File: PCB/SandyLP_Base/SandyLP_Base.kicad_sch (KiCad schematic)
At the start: 173 parts, among them J1 Conn_02x02_Top_Bottom, J11 Conn_02x02_Odd_Even, J2 Conn_02x02_Top_Bottom, J3 Conn_02x02_Top_Bottom, J4 Conn_02x02_Top_Bottom, J5 Conn_02x02_Top_Bottom, J6 Conn_02x02_Top_Bottom, J7 USB_C_Receptacle_USB2.0, J8 Conn_01x03, J9 Conn_01x08_Pin, Q1 BSS138, SW1 BOOT, SW2 RESET, U1 NCP1117-3.3_SOT223, U2 RP2040, U3 W25Q128JVPIQ, Y1 12MHz

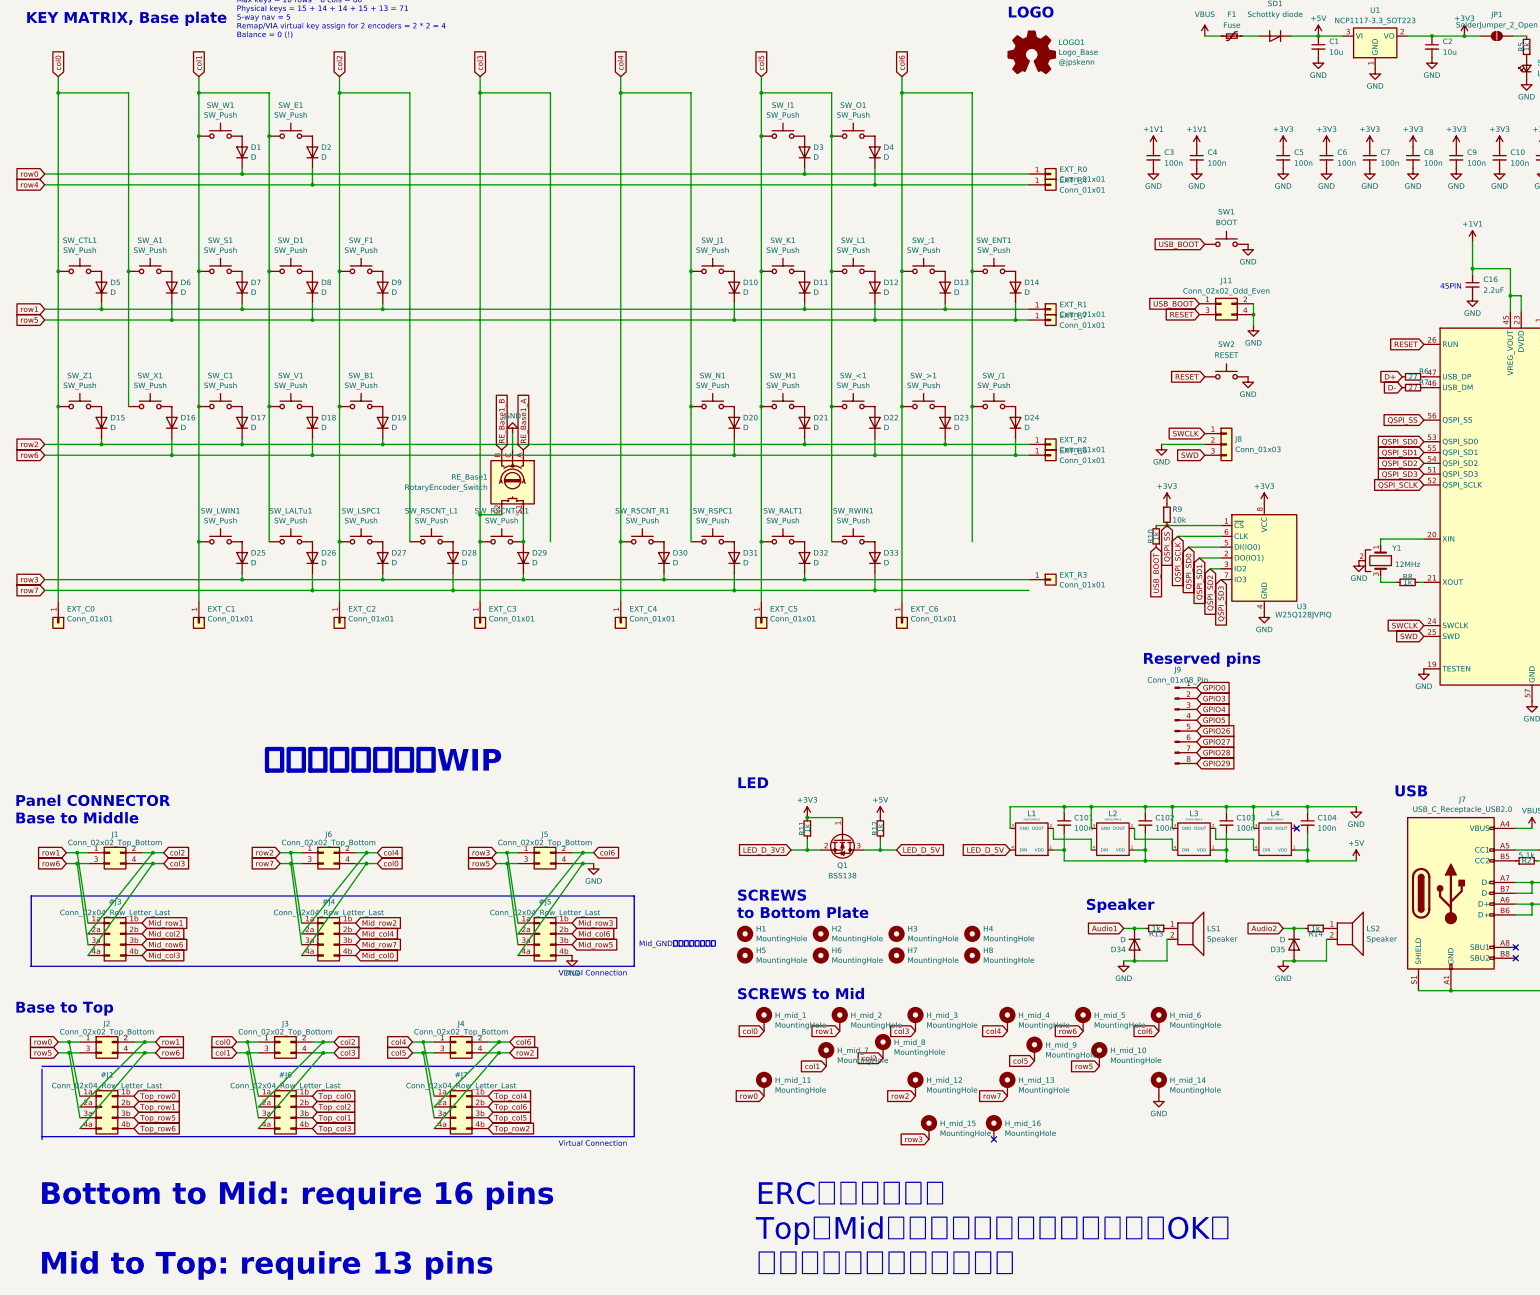
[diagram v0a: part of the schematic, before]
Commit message: 回路図編集：基板間接続、ネジ、フットプリント指定
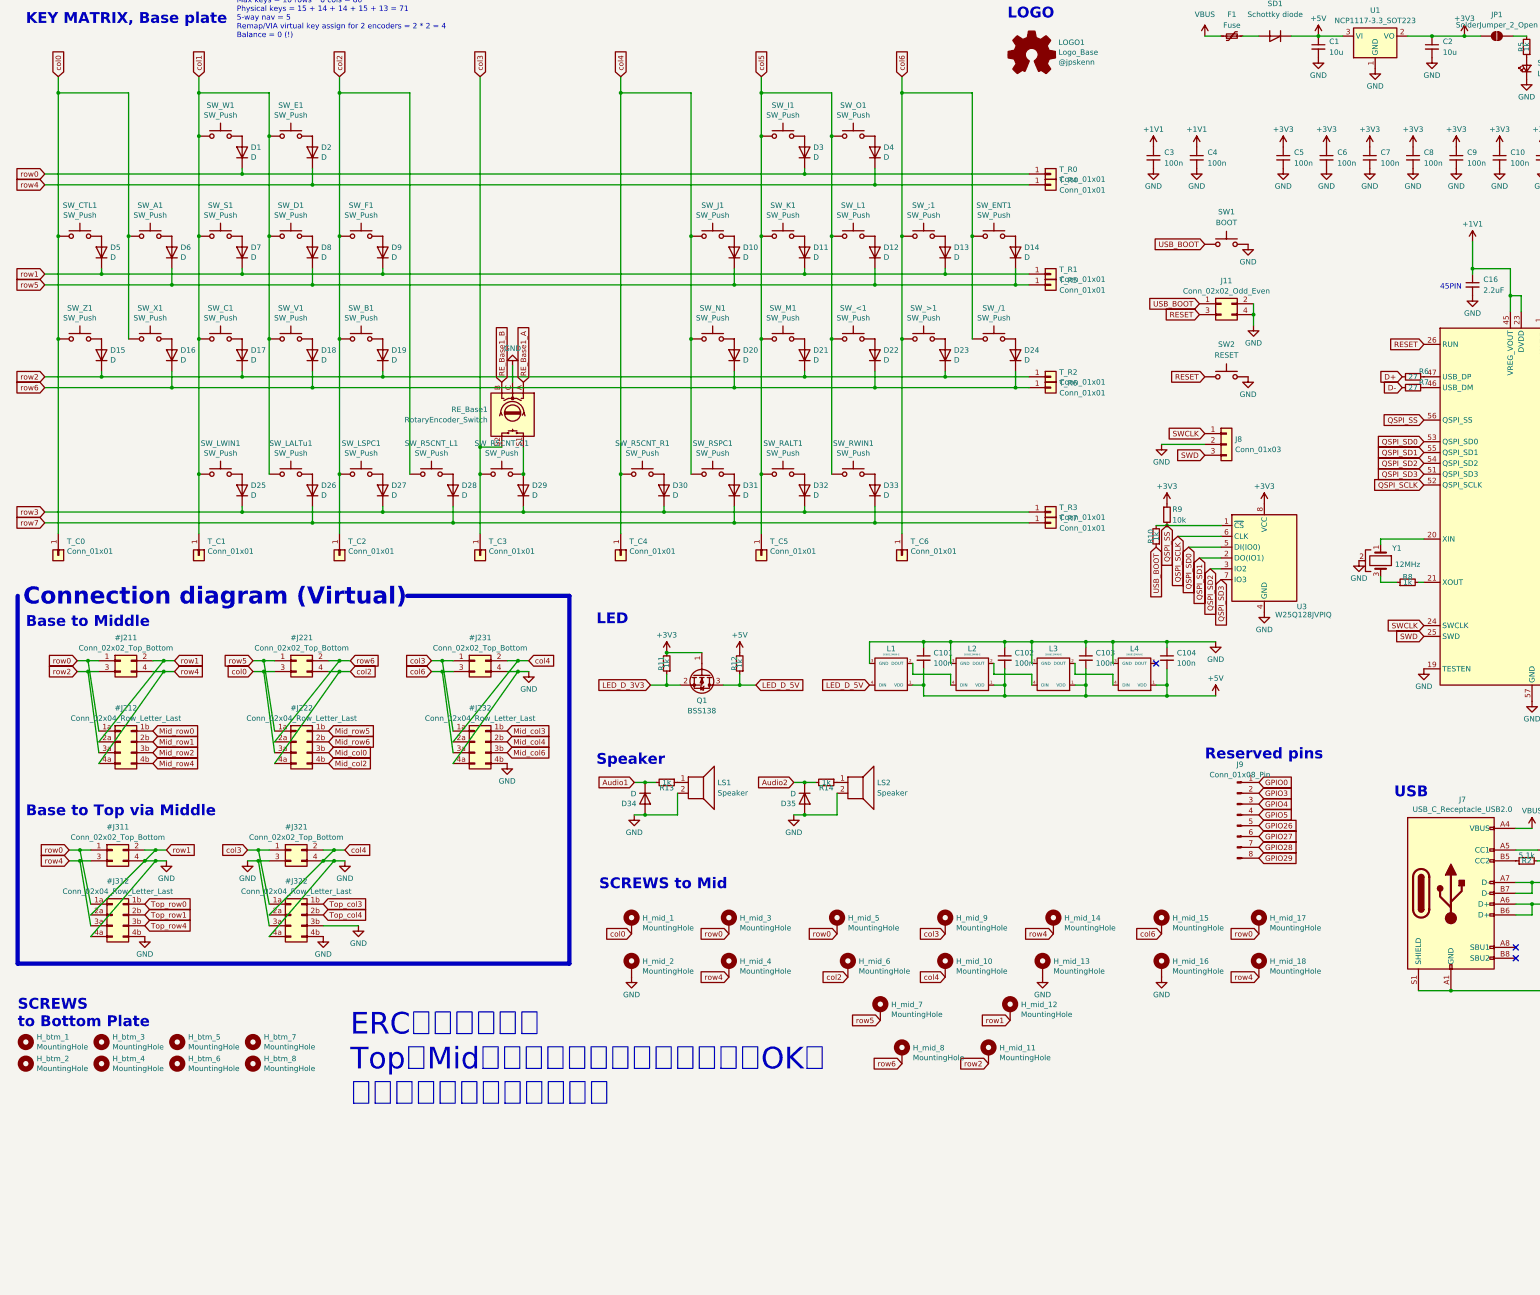
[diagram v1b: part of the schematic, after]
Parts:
- removed #J7: Conn_02x04_Row_Letter_Last, symbol Connector_Generic:Conn_02x04_Row_Letter_Last
- removed H_mid_13, H_mid_15, H_mid_7, H_mid_9: MountingHole, locallib:MountingHole_2.2mm_M2_Pad_minimal, symbol Mechanical:MountingHole_Pad
- removed J4: Conn_02x02_Top_Bottom, locallib:JST_SH_SM04B-SRSS-TB_1x04-1MP_P1.00mm_Horizontal_wCable_housing_spare_pin_courtyard, symbol Connector_Generic:Conn_02x02_Odd_Even
- added H_mid_14, H_mid_17, H_mid_18, H_mid_2, H_mid_3, H_mid_4: MountingHole, locallib:MountingHole_1.8-2.2mm_M2_Pad_minimal, symbol Mechanical:MountingHole_Pad
- added T_R7: Conn_01x01, locallib:TestPoint_THTPad_D2.0mm_Drill1.0mm, symbol Connector_Generic:Conn_01x01
- H_mid_1, H_mid_16: footprint locallib:MountingHole_2.2mm_M2_Pad_minimal -> locallib:MountingHole_1.8-2.2mm_M2_Pad_minimal
- H_mid_10: renamed from H_mid_4; footprint locallib:MountingHole_2.2mm_M2_Pad_minimal -> locallib:MountingHole_1.8-2.2mm_M2_Pad_minimal
- H_mid_11: renamed from H_mid_12; footprint locallib:MountingHole_2.2mm_M2_Pad_minimal -> locallib:MountingHole_1.8-2.2mm_M2_Pad_minimal
- H_mid_12: renamed from H_mid_2; footprint locallib:MountingHole_2.2mm_M2_Pad_minimal -> locallib:MountingHole_1.8-2.2mm_M2_Pad_minimal
- H_mid_13: renamed from H_mid_14; footprint locallib:MountingHole_2.2mm_M2_Pad_minimal -> locallib:MountingHole_1.8-2.2mm_M2_Pad_minimal
- H_mid_15: renamed from H_mid_6; footprint locallib:MountingHole_2.2mm_M2_Pad_minimal -> locallib:MountingHole_1.8-2.2mm_M2_Pad_minimal
- H_mid_5: renamed from H_mid_11; footprint locallib:MountingHole_2.2mm_M2_Pad_minimal -> locallib:MountingHole_1.8-2.2mm_M2_Pad_minimal
- H_mid_6: renamed from H_mid_8; footprint locallib:MountingHole_2.2mm_M2_Pad_minimal -> locallib:MountingHole_1.8-2.2mm_M2_Pad_minimal
- H_mid_7: renamed from H_mid_10; footprint locallib:MountingHole_2.2mm_M2_Pad_minimal -> locallib:MountingHole_1.8-2.2mm_M2_Pad_minimal
- H_mid_8: renamed from H_mid_5; footprint locallib:MountingHole_2.2mm_M2_Pad_minimal -> locallib:MountingHole_1.8-2.2mm_M2_Pad_minimal
- H_mid_9: renamed from H_mid_3; footprint locallib:MountingHole_2.2mm_M2_Pad_minimal -> locallib:MountingHole_1.8-2.2mm_M2_Pad_minimal
- renumbered J1 to #J211, #J3 to #J212, J6 to #J221, #J4 to #J222, J5 to #J231, #J5 to #J232, J2 to #J311, #J1 to #J312, J3 to #J321, #J6 to #J322, H1 to H_btm_1, H5 to H_btm_2, H2 to H_btm_3, H6 to H_btm_4, H3 to H_btm_5, H7 to H_btm_6, H4 to H_btm_7, H8 to H_btm_8, EXT_C0 to T_C0, EXT_C1 to T_C1, EXT_C2 to T_C2, EXT_C3 to T_C3, EXT_C4 to T_C4, EXT_C5 to T_C5, EXT_C6 to T_C6, EXT_R0 to T_R0, EXT_R1 to T_R1, EXT_R2 to T_R2, EXT_R3 to T_R3, EXT_R4 to T_R4, EXT_R7 to T_R5, EXT_R6 to T_R6
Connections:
- net Mid_row3 is gone; now on net Mid_col3: #J232.1b (Pin_1b)
- net Mid_row7 is gone; now on net Mid_col0: #J222.3b (Pin_3b)
- net Top_col0 is gone; now on net Top_col3: #J322.1b (Pin_1b)
- net Top_col1 is gone; now on net GND: #J322.3b (Pin_3b)
- net Top_col2 is gone; now on net Top_col4: #J322.2b (Pin_2b)
- net Top_row6 is gone; now on net GND: #J312.4b (Pin_4b)
- net GND: now also #J211.2 (Pin_2), #J212.2a (Pin_2a), #J231.2 (Pin_2), #J232.2a (Pin_2a), #J311.2 (Pin_2), #J311.4 (Pin_4), #J312.2a (Pin_2a), #J312.4a (Pin_4a), #J321.2 (Pin_2), #J321.3 (Pin_3), #J321.4 (Pin_4), #J322.2a (Pin_2a), #J322.3a (Pin_3a), #J322.4a (Pin_4a), #J322.4b (Pin_4b), D11.1 (K), D13.1 (K), D5.1 (K), D7.1 (K), D9.1 (K), H_mid_10.1, H_mid_12.1, H_mid_16.1, SW_J1.1, SW_N1.1, SW_R5CNT_R1.1, SW_RSPC1.1, T_C4.1 (Pin_1), T_R1.1 (Pin_1), U2.11 (GPIO8), U2.3 (GPIO1), H_mid_2.1
- net Mid_col0: no longer #J222.4b (Pin_4b)
- net Mid_col2: now also #J222.4b (Pin_4b); no longer #J212.2b (Pin_2b)
- net Mid_col3: no longer #J212.4b (Pin_4b)
- net Mid_col4: now also #J232.2b (Pin_2b); no longer #J222.2b (Pin_2b)
- net Mid_col6: now also #J232.3b (Pin_3b); no longer #J232.2b (Pin_2b)
- net Mid_row1: now also #J212.2b (Pin_2b); no longer #J212.1b (Pin_1b)
- net Mid_row2: now also #J212.3b (Pin_3b); no longer #J222.1b (Pin_1b)
- net Mid_row5: now also #J222.1b (Pin_1b); no longer #J232.3b (Pin_3b)
- net Mid_row6: now also #J222.2b (Pin_2b); no longer #J212.3b (Pin_3b)
- net Top_col3: no longer #J322.4b (Pin_4b)
- net col0: now also #J221.3 (Pin_3), #J222.3a (Pin_3a); no longer #J221.4 (Pin_4), #J222.4a (Pin_4a), #J321.1 (Pin_1), #J322.1a (Pin_1a)
- net col1: no longer #J321.3 (Pin_3), #J322.3a (Pin_3a)
- net col2: now also #J221.4 (Pin_4), #J222.4a (Pin_4a); no longer #J211.2 (Pin_2), #J212.2a (Pin_2a), #J321.2 (Pin_2), #J322.2a (Pin_2a)
- net col3: now also #J231.1 (Pin_1), #J232.1a (Pin_1a), #J321.1 (Pin_1), #J322.1a (Pin_1a); no longer #J211.4 (Pin_4), #J212.4a (Pin_4a), #J321.4 (Pin_4), #J322.4a (Pin_4a)
- net col6: now also #J231.3 (Pin_3), #J232.3a (Pin_3a); no longer #J231.2 (Pin_2), #J232.2a (Pin_2a)
- net row0: now also #J211.1 (Pin_1), #J212.1a (Pin_1a), H_mid_17.1, H_mid_3.1
- net row2: now also #J211.3 (Pin_3), #J212.3a (Pin_3a); no longer #J221.1 (Pin_1), #J222.1a (Pin_1a)
- net row3: no longer #J231.1 (Pin_1), #J232.1a (Pin_1a)
- net row4: now also #J211.4 (Pin_4), #J212.4a (Pin_4a), #J311.3 (Pin_3), #J312.3a (Pin_3a), H_mid_14.1, H_mid_18.1, H_mid_4.1
- net row5: now also #J221.1 (Pin_1), #J222.1a (Pin_1a); no longer #J231.3 (Pin_3), #J232.3a (Pin_3a), #J311.3 (Pin_3), #J312.3a (Pin_3a)
- net row6: now also #J221.2 (Pin_2), #J222.2a (Pin_2a); no longer #J211.3 (Pin_3), #J212.3a (Pin_3a), #J311.4 (Pin_4), #J312.4a (Pin_4a)
- net row7: now also T_R7.1 (Pin_1); no longer #J221.3 (Pin_3), #J222.3a (Pin_3a)
- net Top_row5 renamed Top_row4
- removed net col4: #J221.2 (Pin_2), #J222.2a (Pin_2a), H_mid_10.1, SW_J1.1, SW_N1.1, SW_R5CNT_R1.1, SW_RSPC1.1, T_C4.1 (Pin_1), U2.3 (GPIO1)
- removed net row1: #J211.1 (Pin_1), #J212.1a (Pin_1a), #J311.2 (Pin_2), #J312.2a (Pin_2a), D11.1 (K), D13.1 (K), D5.1 (K), D7.1 (K), D9.1 (K), H_mid_12.1, T_R1.1 (Pin_1), U2.11 (GPIO8)
- new net Mid_row0: #J212.1b (Pin_1b)
- new net Mid_row4: #J212.4b (Pin_4b)
- no-connect marks 4 -> 3
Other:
- note added: "Base to Middle"
- note added: "Base to Top via Middle"
- note added: "Connection diagram (Virtual)"
- note removed: "Base to Top"
- note removed: "Bottom to Mid: require 16 pins Mid to Top: require 13 pins"
- note removed: "Mid_GNDを仮につけている"
- note removed: "Panel CONNECTOR Base to Middle"
- note removed: "Virtual Connection"
- note removed: "コネクタとネジはWIP"
- moved on the sheet: C101, C102, C103, C104, D10, D11, D12, D13, D14, D15, D16, D17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

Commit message: Base外形作成。ネジ配置。
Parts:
- removed J9: Conn_01x08_Pin, locallib:PinHeader_1x08_P1.00mm_Vertical_All_circle, symbol Connector:Conn_01x08_Pin
- added J1: Conn_01x09_Pin, symbol Connector:Conn_01x09_Pin
- renumbered H_mid_6 to H_mid_10, H_mid_10 to H_mid_11, H_mid_13 to H_mid_12, H_mid_16 to H_mid_13, H_mid_18 to H_mid_14, H_mid_7 to H_mid_15, H_mid_12 to H_mid_16, H_mid_8 to H_mid_17, H_mid_11 to H_mid_18, H_mid_3 to H_mid_2, H_mid_5 to H_mid_3, H_mid_9 to H_mid_4, H_mid_14 to H_mid_5, H_mid_15 to H_mid_6, H_mid_17 to H_mid_7, H_mid_2 to H_mid_8, H_mid_4 to H_mid_9
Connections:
- net GND: now also H_mid_14.1; no longer #J211.2 (Pin_2), #J212.2a (Pin_2a), #J231.2 (Pin_2), #J232.2a (Pin_2a), #J311.2 (Pin_2), #J312.2a (Pin_2a), #J321.2 (Pin_2), #J322.2a (Pin_2a), D11.1 (K), D13.1 (K), D5.1 (K), D7.1 (K), D9.1 (K), H_mid_11.1, H_mid_13.1, H_mid_16.1, SW_J1.1, SW_N1.1, SW_R5CNT_R1.1, SW_RSPC1.1, T_C4.1 (Pin_1), T_R1.1 (Pin_1), U2.11 (GPIO8), U2.3 (GPIO1)
- net GPIO0: now also J1.1 (Pin_1)
- net GPIO14: now also J1.5 (Pin_5)
- net GPIO26: now also J1.6 (Pin_6)
- net GPIO27: now also J1.7 (Pin_7)
- net GPIO28: now also J1.8 (Pin_8)
- net GPIO29: now also J1.9 (Pin_9)
- net GPIO3: now also J1.2 (Pin_2)
- net GPIO4: now also J1.3 (Pin_3)
- net GPIO5: now also J1.4 (Pin_4)
- net col6: now also H_mid_7.1; no longer H_mid_6.1
- net row0: now also H_mid_6.1; no longer H_mid_7.1
- net row4: now also H_mid_13.1; no longer H_mid_14.1
- new net col4: #J231.2 (Pin_2), #J232.2a (Pin_2a), #J321.2 (Pin_2), #J322.2a (Pin_2a), H_mid_11.1, SW_J1.1, SW_N1.1, SW_R5CNT_R1.1, SW_RSPC1.1, T_C4.1 (Pin_1), U2.3 (GPIO1)
- new net row1: #J211.2 (Pin_2), #J212.2a (Pin_2a), #J311.2 (Pin_2), #J312.2a (Pin_2a), D11.1 (K), D13.1 (K), D5.1 (K), D7.1 (K), D9.1 (K), H_mid_16.1, T_R1.1 (Pin_1), U2.11 (GPIO8)

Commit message: WIP パーツ配置
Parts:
- removed C101, C102, C103, C104: 100n, Capacitor_SMD:C_0402_1005Metric, symbol Device:C_Small
- added C14, C15, C18, C19, C20, C21: 100n, Capacitor_SMD:C_0402_1005Metric, symbol Device:C_Small
- added L5, L6: SK6812MINI-E, locallib:YS-SK6812MINI-E_middle_hole_with_small_pad, symbol kbd:SK6812MINI-E
- J1: footprint (none) -> Connector_PinHeader_1.00mm:PinHeader_1x09_P1.00mm_Vertical
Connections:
- net +5V: now also C14.2, C15.2, C18.2, C19.2, C20.2, C21.2, L5.1 (VDD), L6.1 (VDD)
- net GND: now also C14.1, C15.1, C18.1, C19.1, C20.1, C21.1, L5.3 (GND), L6.3 (GND)
- net LED_D_5V_CONNECTION: now reaches L3.2 (DOUT), L4.4 (DIN)
- net at L4.2 (DOUT): now also L5.4 (DIN)
- new net: L5.2 (DOUT), L6.4 (DIN)

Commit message: USBコネクタ周りの配線に合わせて、Mid孤立部分のネジへのピン割り当てを変更。
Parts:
- LOGO1: footprint Jones.local:Sandy_logo_w60_new -> locallib:SandyLP_logo_w60
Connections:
- net GND: now also H_mid_13.1, H_mid_9.1; no longer H_mid_14.1, H_mid_8.1
- net row4: now also H_mid_14.1, H_mid_8.1; no longer H_mid_13.1, H_mid_9.1
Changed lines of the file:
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@@
 	(global_label "row4"
 		(shape input)
-		(at 180.34 243.84 180)
+		(at 157.48 243.84 180)
 		(fields_autoplaced yes)
 		(effects
@@
 		)
 		(property "Intersheetrefs" "${INTERSHEET_REFS}"
-			(at 173.5338 243.84 0)
+			(at 150.6738 243.84 0)
 			(effects
 				(font
@@
 		)
 		(property "シート間のリファレンス" "${INTERSHEET_REFS}"
-			(at 180.34 245.6752 0)
+			(at 157.48 245.6752 0)
 			(effects
 				(font
@@
 	(global_label "row4"
 		(shape input)
-		(at 281.94 243.84 180)
+		(at 304.8 243.84 180)
 		(fields_autoplaced yes)
 		(effects
@@
 		)
 		(property "Intersheetrefs" "${INTERSHEET_REFS}"
-			(at 275.1338 243.84 0)
+			(at 297.9938 243.84 0)
 			(effects
 				(font
@@
 		)
 		(property "シート間のリファレンス" "${INTERSHEET_REFS}"
-			(at 281.94 245.6752 0)
+			(at 304.8 245.6752 0)
 			(effects
 				(font
@@
 			)
 		)
-		(property "Footprint" "Jones.local:Sandy_logo_w60_new"
+		(property "Footprint" "locallib:SandyLP_logo_w60"
 			(at 251.46 27.305 0)
 			(effects
@@
 	(symbol
 		(lib_id "power:GND")
-		(at 304.8 243.84 0)
+		(at 281.94 243.84 0)
 		(unit 1)
 		(exclude_from_sim no)
@@
 		(fields_autoplaced yes)
 		(property "Reference" "#PWR067"
-			(at 304.8 250.19 0)
+			(at 281.94 250.19 0)
 			(effects
 				(font
@@
 		)
 		(property "Value" "GND"
-			(at 304.8 247.9731 0)
+			(at 281.94 247.9731 0)
 			(effects
 				(font
@@
 		)
 		(property "Footprint" ""
-			(at 304.8 243.84 0)
+			(at 281.94 243.84 0)
 			(effects
 				(font
@@
 		)
 		(property "Datasheet" ""
-			(at 304.8 243.84 0)
+			(at 281.94 243.84 0)
 			(effects
 				(font
@@
 		)
 		(property "Description" "Power symbol creates a global label with name \"GND\" , ground"
-			(at 304.8 243.84 0)
+			(at 281.94 243.84 0)
 			(effects
 				(font
@@
 	(symbol
 		(lib_id "power:GND")
-		(at 157.48 243.84 0)
+		(at 180.34 243.84 0)
 		(unit 1)
 		(exclude_from_sim no)
@@
 		(fields_autoplaced yes)
 		(property "Reference" "#PWR066"
-			(at 157.48 250.19 0)
+			(at 180.34 250.19 0)
 			(effects
 				(font
@@
 		)
 		(property "Value" "GND"
-			(at 157.48 247.9731 0)
+			(at 180.34 247.9731 0)
 			(effects
 				(font
@@
 		)
 		(property "Footprint" ""
-			(at 157.48 243.84 0)
+			(at 180.34 243.84 0)
 			(effects
 				(font
@@
 		)
 		(property "Datasheet" ""
-			(at 157.48 243.84 0)
+			(at 180.34 243.84 0)
 			(effects
 				(font
@@
 		)
 		(property "Description" "Power symbol creates a global label with name \"GND\" , ground"
-			(at 157.48 243.84 0)
+			(at 180.34 243.84 0)
 			(effects
 				(font

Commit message: 配線完了。ビア打ちまだ。
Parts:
- removed J1: Conn_01x09_Pin, Connector_PinHeader_1.00mm:PinHeader_1x09_P1.00mm_Vertical, symbol Connector:Conn_01x09_Pin
- removed SW_R5CNT_C1: SW_Push, locallib:Kailh_socket_ChocV2, symbol Switch:SW_Push
- added H_btm_5, H_btm_6, H_btm_7: MountingHole, locallib:MountingHole_2.2mm_M2_No_Cu, symbol Mechanical:MountingHole
- added J1: Conn_01x10_Pin, Connector_PinHeader_1.00mm:PinHeader_1x10_P1.00mm_Vertical, symbol Connector:Conn_01x10_Pin
- SW1, SW2: footprint Button_Switch_SMD:SW_SPST_PTS810 -> Button_Switch_SMD:SW_SPST_TL3342
- SW_R5CNT_C1: renamed from RE_Base1; footprint locallib:RotaryEncoder_Alps_EC11K-Switch_Vertical_H20mm_NPTH_MP_minimal -> locallib:ChocV2_AND_RotaryEncoder_Alps_EC11K-Switch_Vertical_H20mm_NPTH_MP_minimal
- renumbered J11 to #J11, H_btm_6 to H_btm_10, H_btm_8 to H_btm_11, H_btm_3 to H_btm_2, H_btm_5 to H_btm_3, H_btm_7 to H_btm_4, H_btm_2 to H_btm_8, H_btm_4 to H_btm_9
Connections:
- net GPIO0 is gone; now on net GPIO29: U2.41 (GPIO29_ADC3)
- net GPIO14 is gone; now on net LED_D_3V3: U2.30 (GPIO19)
- net GPIO3 is gone; now on net GPIO28: U2.40 (GPIO28_ADC2)
- net GPIO4 is gone; now on net GPIO27: U2.39 (GPIO27_ADC1)
- net Audio1: now also U2.29 (GPIO18); no longer U2.31 (GPIO20)
- net Audio2: now also U2.15 (GPIO12); no longer U2.13 (GPIO10)
- net GPIO26: now also U2.38 (GPIO26_ADC0), J1.7 (Pin_7); no longer U2.37 (GPIO25)
- net GPIO27: now also J1.8 (Pin_8); no longer U2.36 (GPIO24)
- net GPIO28: now also J1.9 (Pin_9); no longer U2.35 (GPIO23)
- net GPIO29: now also J1.10 (Pin_10); no longer U2.34 (GPIO22)
- net LED_D_3V3: no longer U2.32 (GPIO21)
- net RE_Base1_A: now also U2.14 (GPIO11); no longer U2.15 (GPIO12)
- net RE_Base1_B: now also U2.13 (GPIO10); no longer U2.14 (GPIO11)
- net col1: now also U2.6 (GPIO4); no longer U2.8 (GPIO6)
- net col2: now also U2.8 (GPIO6); no longer U2.9 (GPIO7)
- net col3: now also SW_R5CNT_C1.S1, U2.7 (GPIO5); no longer SW_R5CNT_C1.S2, U2.2 (GPIO0)
- net col4: now also U2.9 (GPIO7); no longer U2.3 (GPIO1)
- net col5: now also U2.4 (GPIO2); no longer U2.7 (GPIO5)
- net col6: now also U2.5 (GPIO3); no longer U2.4 (GPIO2)
- net row0: now also U2.2 (GPIO0); no longer U2.5 (GPIO3)
- net row2: now also U2.28 (GPIO17); no longer U2.27 (GPIO16)
- net row3: now also U2.16 (GPIO13); no longer U2.29 (GPIO18)
- net row4: now also U2.3 (GPIO1); no longer U2.16 (GPIO13)
- net row5: now also U2.12 (GPIO9); no longer U2.6 (GPIO4)
- net row6: now also U2.27 (GPIO16); no longer U2.12 (GPIO9)
- net row7: now also U2.17 (GPIO14); no longer U2.28 (GPIO17)
- net at D29.2 (A): now also SW_R5CNT_C1.S2; no longer SW_R5CNT_C1.S1
- removed net GPIO5: U2.17 (GPIO14), U2.38 (GPIO26_ADC0)
- new net GPIO20: J1.1 (Pin_1), U2.31 (GPIO20)
- new net GPIO21: J1.2 (Pin_2), U2.32 (GPIO21)
- new net GPIO22: J1.3 (Pin_3), U2.34 (GPIO22)
- new net GPIO23: J1.4 (Pin_4), U2.35 (GPIO23)
- new net GPIO24: J1.5 (Pin_5), U2.36 (GPIO24)
- new net GPIO25: J1.6 (Pin_6), U2.37 (GPIO25)
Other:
- moved on the sheet: H_btm_10, H_btm_11, H_btm_8, H_btm_9, SW_R5CNT_C1

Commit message: 製造用ファイル出力
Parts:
- D1, D10, D11, D12, D13, D14, D15, D16, D17, D18, D19, D2, D20, D21, D22, D23, D24, D25, D26, D27, D28, D29, D3, D30, D31, D32, D33, D34, D35, D4, D5, D6, D7, D8, D9: LCSC C109203 -> C81598
- LS1, LS2: LCSC C910763 -> (none); LCSC-Reserve (none) -> C910763
- SW1, SW2: LCSC C92589 -> (none); LCSC-Reserve (none) -> C2886897
